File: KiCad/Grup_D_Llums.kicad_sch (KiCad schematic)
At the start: 0 parts

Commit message: Sensor llums afegit
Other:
- sheet Sheet_d renamed Sensor_Llums
- sheet Sensor_Llums: file Sheet_d.kicad_sch -> Sensor_LLums.kicad_sch
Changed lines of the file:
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@@
 			(color 0 0 0 0.0000)
 		)
-		(property "Sheetname" "Sheet_d"
+		(property "Sheetname" "Sensor_Llums"
 			(at 22.86 70.4084 0)
 			(effects
@@
 			)
 		)
-		(property "Sheetfile" "Sheet_d.kicad_sch"
+		(property "Sheetfile" "Sensor_LLums.kicad_sch"
 			(at 22.86 107.2646 0)
 			(effects

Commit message: Nada
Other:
- sheet Sheet_e renamed Drivers_Llums
- sheet Drivers_Llums: file Sheet_e.kicad_sch -> Drivers_Llums.kicad_sch
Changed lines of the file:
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@@
 			(color 0 0 0 0.0000)
 		)
-		(property "Sheetname" "Sheet_e"
+		(property "Sheetname" "Drivers_Llums"
 			(at 91.44 70.4084 0)
 			(effects
@@
 			)
 		)
-		(property "Sheetfile" "Sheet_e.kicad_sch"
+		(property "Sheetfile" "Drivers_Llums.kicad_sch"
 			(at 91.44 107.2646 0)
 			(effects

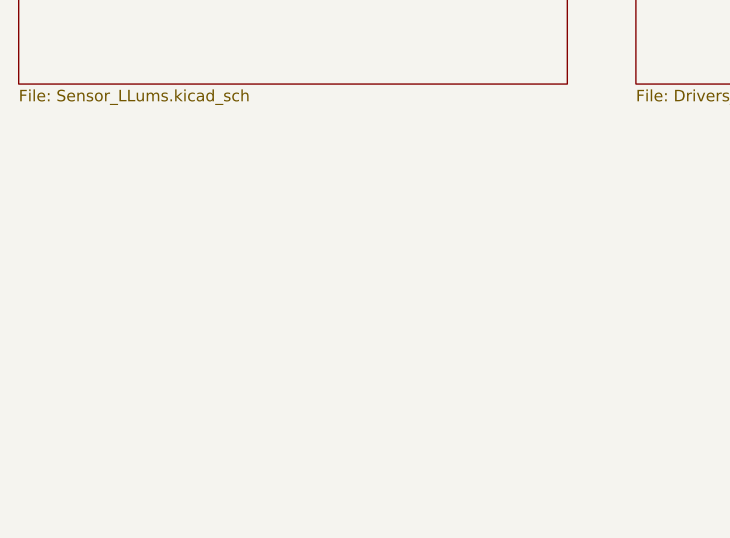
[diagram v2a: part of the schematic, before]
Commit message: Communicacio afegida
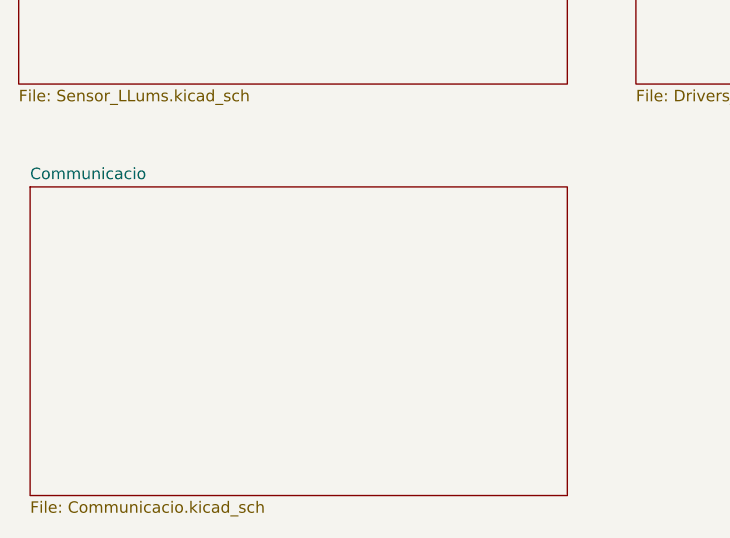
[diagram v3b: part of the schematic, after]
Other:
- added sheet Communicacio (Communicacio.kicad_sch)
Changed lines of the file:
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@@
+		)
+	)
+	(sheet
+		(at 24.13 118.11)
+		(size 59.69 34.29)
+		(exclude_from_sim no)
+		(in_bom yes)
+		(on_board yes)
+		(dnp no)
+		(fields_autoplaced yes)
+		(stroke
+			(width 0.1524)
+			(type solid)
+		)
+		(fill
+			(color 0 0 0 0.0000)
+		)
+		(property "Sheetname" "Communicacio"
+			(at 24.13 117.3984 0)
+			(effects
+				(font
+					(size 1.27 1.27)
+				)
+				(justify left bottom)
+			)
+		)
+		(property "Sheetfile" "Communicacio.kicad_sch"
+			(at 24.13 152.9846 0)
+			(effects
+				(font
+					(size 1.27 1.27)
+				)
+				(justify left top)
+			)
+		)
+		(instances
+			(project "Grup_D_Llums"
+				(path "/88ef36bc-9439-47f2-adb5-e1da6bb8c9dd"
+					(page "8")
+				)
+			)
 		)
 	)

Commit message: Procesament i comunicació
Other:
- sheet Sheet_f renamed Procesament
- sheet Procesament: file Sheet_f.kicad_sch -> Procesament.kicad_sch
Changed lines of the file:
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@@
 			(color 0 0 0 0.0000)
 		)
-		(property "Sheetname" "Sheet_f"
+		(property "Sheetname" "Procesament"
 			(at 161.29 70.4084 0)
 			(effects
@@
 			)
 		)
-		(property "Sheetfile" "Sheet_f.kicad_sch"
+		(property "Sheetfile" "Procesament.kicad_sch"
 			(at 161.29 107.2646 0)
 			(effects

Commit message: Arreglat errors de schematic version 1
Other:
- sheet Alimentacio renamed POTENCIA
- sheet Drivers_Llums renamed LLUMS
- removed sheet Drivers_Motor
- removed sheet Sensor_Llums
- sheet LLUMS: file Drivers_Llums.kicad_sch -> LLUMS.kicad_sch
- sheet POTENCIA: file Alimentacio.kicad_sch -> POTENCIA.kicad_sch
- note added: "LLUMS"
- note added: "POTENCIA"
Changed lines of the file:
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@@
 		(date "2026-03-16")
 	)
-	(sheet
-		(at 161.29 26.67)
-		(size 60.96 35.56)
-		(exclude_from_sim no)
-		(in_bom yes)
-		(on_board yes)
-		(dnp no)
-		(fields_autoplaced yes)
-		(stroke
-			(width 0.1524)
-			(type solid)
-		)
-		(fill
-			(color 0 0 0 0.0000)
-		)
-		(property "Sheetname" "Drivers_Motor"
-			(at 161.29 25.9584 0)
-			(effects
-				(font
-					(size 1.27 1.27)
-				)
-				(justify left bottom)
-			)
-		)
-		(property "Sheetfile" "Drivers_motor.kicad_sch"
-			(at 161.29 62.8146 0)
-			(effects
-				(font
-					(size 1.27 1.27)
-				)
-				(justify left top)
-			)
-		)
-		(instances
-			(project "Grup_D_Llums"
-				(path "/88ef36bc-9439-47f2-adb5-e1da6bb8c9dd"
-					(page "2")
-				)
+	(text "LLUMS\n"
+		(exclude_from_sim no)
+		(at 120.396 89.662 0)
+		(effects
+			(font
+				(size 3.81 3.81)
+			)
+		)
+	)
+	(text "POTENCIA"
+		(exclude_from_sim no)
+		(at 51.308 45.212 0)
+		(effects
+			(font
+				(size 3.81 3.81)
 			)
 		)
@@
 			(color 0 0 0 0.0000)
 		)
-		(property "Sheetname" "Drivers_Llums"
+		(property "Sheetname" "LLUMS"
 			(at 91.44 70.4084 0)
 			(effects
@@
 			)
 		)
-		(property "Sheetfile" "Drivers_Llums.kicad_sch"
+		(property "Sheetfile" "LLUMS.kicad_sch"
 			(at 91.44 107.2646 0)
 			(effects
@@
 				(path "/88ef36bc-9439-47f2-adb5-e1da6bb8c9dd"
 					(page "7")
-				)
-			)
-		)
-	)
-	(sheet
-		(at 22.86 71.12)
-		(size 60.96 35.56)
-		(exclude_from_sim no)
-		(in_bom yes)
-		(on_board yes)
-		(dnp no)
-		(fields_autoplaced yes)
-		(stroke
-			(width 0.1524)
-			(type solid)
-		)
-		(fill
-			(color 0 0 0 0.0000)
-		)
-		(property "Sheetname" "Sensor_Llums"
-			(at 22.86 70.4084 0)
-			(effects
-				(font
-					(size 1.27 1.27)
-				)
-				(justify left bottom)
-			)
-		)
-		(property "Sheetfile" "Sensor_LLums.kicad_sch"
-			(at 22.86 107.2646 0)
-			(effects
-				(font
-					(size 1.27 1.27)
-				)
-				(justify left top)
-			)
-		)
-		(instances
-			(project "Grup_D_Llums"
-				(path "/88ef36bc-9439-47f2-adb5-e1da6bb8c9dd"
-					(page "5")
 				)
 			)
@@
 			(color 0 0 0 0.0000)
 		)
-		(property "Sheetname" "Alimentacio"
+		(property "Sheetname" "POTENCIA"
 			(at 24.13 25.9584 0)
 			(effects
@@
 			)
 		)
-		(property "Sheetfile" "Alimentacio.kicad_sch"
+		(property "Sheetfile" "POTENCIA.kicad_sch"
 			(at 24.13 62.8146 0)
 			(effects
@@
 	)
 	(sheet
-		(at 24.13 118.11)
+		(at 22.86 72.39)
 		(size 59.69 34.29)
 		(exclude_from_sim no)
@@
 		)
 		(property "Sheetname" "Communicacio"
-			(at 24.13 117.3984 0)
+			(at 22.86 71.6784 0)
 			(effects
 				(font
@@
 		)
 		(property "Sheetfile" "Communicacio.kicad_sch"
-			(at 24.13 152.9846 0)
-			(effects
-				(font
+			(at 22.86 107.2646 0)
+			(effects
+				(font

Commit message: Bloc processament
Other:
- removed sheet Communicacio
- removed sheet Procesament
- note added: "PROCESSAMENT"
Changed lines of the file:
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@@
 		(date "2026-03-16")
+	)
+	(text "PROCESSAMENT\n"
+		(exclude_from_sim no)
+		(at 121.92 42.672 0)
+		(effects
+			(font
+				(size 3.81 3.81)
+			)
+		)
 	)
 	(text "LLUMS\n"
 		(exclude_from_sim no)
-		(at 120.396 89.662 0)
+		(at 51.816 93.472 0)
 		(effects
 			(font
@@
 	)
 	(sheet
-		(at 91.44 71.12)
+		(at 22.86 74.93)
 		(size 60.96 35.56)
 		(exclude_from_sim no)
@@
 		)
 		(property "Sheetname" "LLUMS"
-			(at 91.44 70.4084 0)
+			(at 22.86 74.2184 0)
 			(effects
 				(font
@@
 		)
 		(property "Sheetfile" "LLUMS.kicad_sch"
-			(at 91.44 107.2646 0)
+			(at 22.86 111.0746 0)
 			(effects
 				(font
@@
 	)
 	(sheet
-		(at 161.29 71.12)
-		(size 60.96 35.56)
-		(exclude_from_sim no)
-		(in_bom yes)
-		(on_board yes)
-		(dnp no)
-		(fields_autoplaced yes)
-		(stroke
-			(width 0.1524)
-			(type solid)
-		)
-		(fill
-			(color 0 0 0 0.0000)
-		)
-		(property "Sheetname" "Procesament"
-			(at 161.29 70.4084 0)
-			(effects
-				(font
-					(size 1.27 1.27)
-				)
-				(justify left bottom)
-			)
-		)
-		(property "Sheetfile" "Procesament.kicad_sch"
-			(at 161.29 107.2646 0)
-			(effects
-				(font
-					(size 1.27 1.27)
-				)
-				(justify left top)
-			)
-		)
-		(instances
-			(project "Grup_D_Llums"
-				(path "/88ef36bc-9439-47f2-adb5-e1da6bb8c9dd"
-					(page "6")
-				)
-			)
-		)
-	)
-	(sheet
 		(at 91.44 26.67)
 		(size 60.96 35.56)
@@
 				)
 			)
-		)
-	)
-	(sheet
-		(at 22.86 72.39)
-		(size 59.69 34.29)
-		(exclude_from_sim no)
-		(in_bom yes)
-		(on_board yes)
-		(dnp no)
-		(fields_autoplaced yes)
-		(stroke
-			(width 0.1524)
-			(type solid)
-		)
-		(fill
-			(color 0 0 0 0.0000)
-		)
-		(property "Sheetname" "Communicacio"
-			(at 22.86 71.6784 0)
-			(effects
-				(font
-					(size 1.27 1.27)
-				)
-				(justify left bottom)
-			)
-		)
-		(property "Sheetfile" "Communicacio.kicad_sch"
-			(at 22.86 107.2646 0)
-			(effects
-				(font
-					(size 1.27 1.27)
-				)
-				(justify left top)
-			)
-		)
-		(instances
-			(project "Grup_D_Llums"
-				(path "/88ef36bc-9439-47f2-adb5-e1da6bb8c9dd"
-					(page "8")
-				)
-			)

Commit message: Finished
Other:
- company: (none) -> Marcel Lleonart, Eric Ruiz, Josep Leyva
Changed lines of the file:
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@@
 		(title "edd-project-grup-dimecres-dc_d_llums")
 		(date "2026-03-16")
+		(rev "28/04/2026")
+		(company "Marcel Lleonart, Eric Ruiz, Josep Leyva")
 	)
 	(text "PROCESSAMENT\n"
